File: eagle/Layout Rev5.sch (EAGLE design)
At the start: 12 parts, among them Q1 TIP122

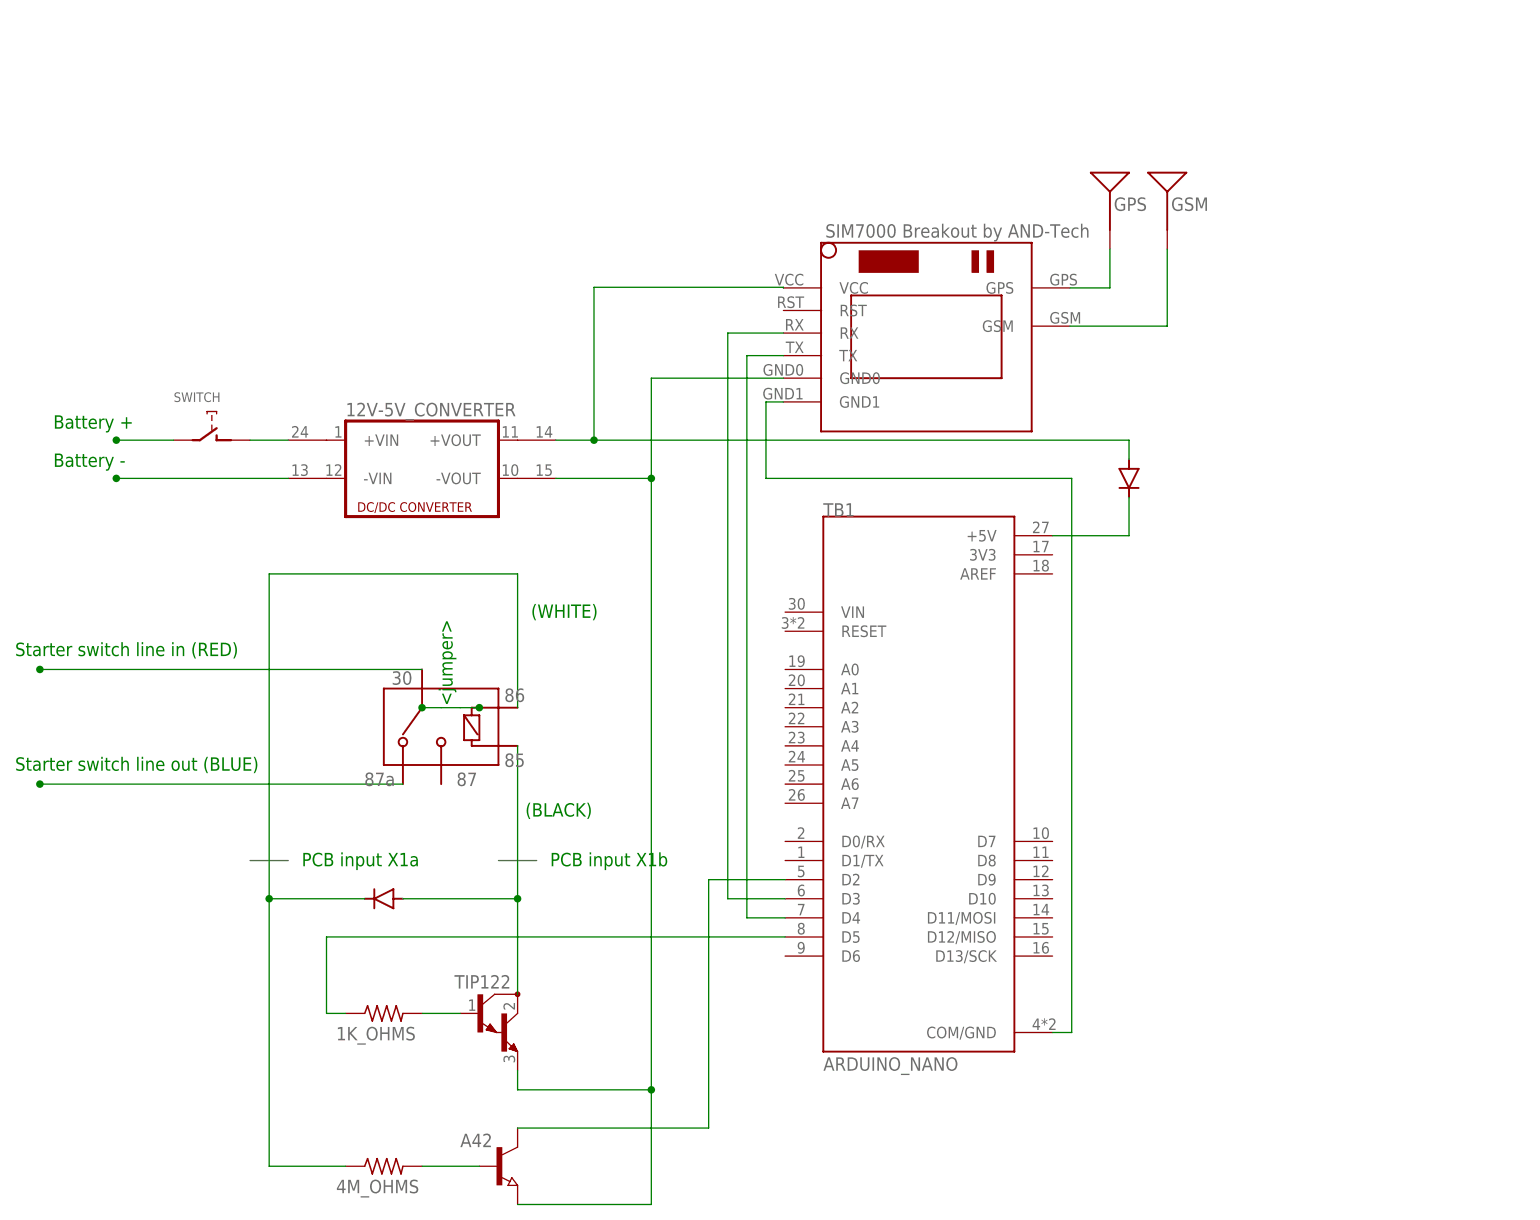
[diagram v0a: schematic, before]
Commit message: both bostig and stock: 1.change 10K resistor to 4M Ohm 2.make wiring look more like reality so building the hardware is more clear/intuitive including adding jumpers and inputs to PCB
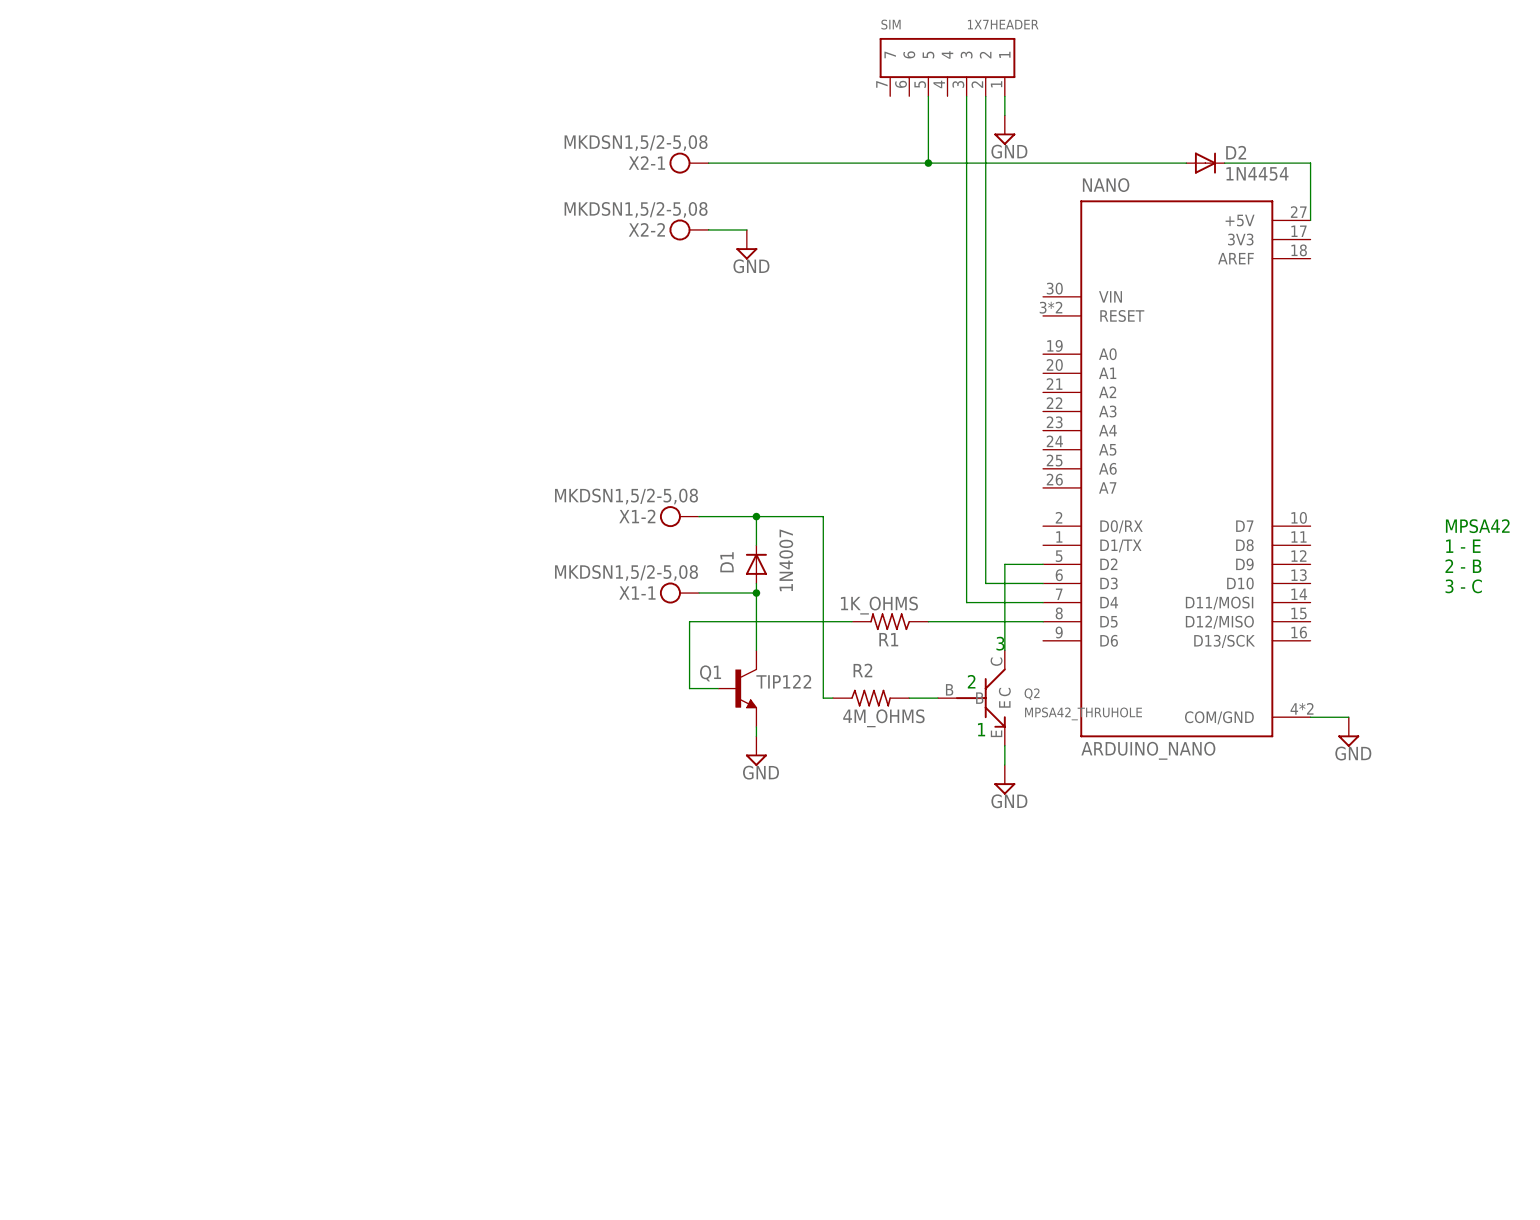
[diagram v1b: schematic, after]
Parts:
- removed 12V-5V_CONVERTER: (no value), dc-dc-converter:DC213R
- removed 1K_OHMS, 4M_OHMS: (no value), rcl:R-US_0411/15
- removed A42: (no value), semicon-smd-ipc:NPN-TRANSISTOR_SOT23
- removed GPS, GSM: 1.575GHz, SparkFun-GPS:ANTENNAGPS-2X7MM
- removed SWITCH: EC12E_SW, switch-alps:EC12E_SW
- removed TB1: ARDUINO_NANO, ARDUINO_NANO:ARDUINO_NANO
- removed U$1: SIM800LMODULE, JW_SIM800LMODULE:SIM800LMODULE
- added NANO: ARDUINO_NANO, ARDUINO_NANO:ARDUINO_NANO
- added Q2: MPSA42_THRUHOLE, MPSA42_thruhole:MPSA42_THRUHOLE
- added R1: 1K_OHMS, rcl:R-US_0207/10
- added R2: 4M_OHMS, rcl:R-US_0207/10
- added SIM: 1X7HEADER, 1x7header:1X7HEADER
- added X1, X2: MKDSN1,5/2-5,08, con-phoenix-508:MKDSN1,5/2-5,08
- D1: value 1N5400 -> 1N4007; device diode:1N5400 -> diode:1N4004
- D2: value 1N5400 -> 1N4454; device diode:1N5400 -> diode:1N4004
- Q1: device transistor-npn:TIP122 -> transistor:2SC1306
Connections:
- removed net N$11: TB1.D3, U$1.RX
- removed net N$12: TB1.D4, U$1.TX
- removed net N$13: 12V-5V_CONVERTER.+VIN1, SWITCHG$2.1
- removed net N$14: 4M_OHMS.2, A42.B
- removed net N$17: 4M_OHMS.1, D1.C
- removed net N$22: TB1.COM/GND, U$1.GND1
- removed net N$23: 12V-5V_CONVERTER.-VOUT1, A42.E, Q1.E, U$1.GND0
- removed net N$6: 1K_OHMS.1, TB1.D5
- removed net N$9: 12V-5V_CONVERTER.+VOUT1, D2.A, U$1.VCC
- new net +5V: D2.A, SIM.5, X2-1.KL
- new net GND: NANO.COM/GND, Q1.E, Q2.E, SIM.1, X2-2.KL
- new net N$7: Q2.B, R2.2
- net N$1: now also NANO.D4, SIM.3; no longer SWITCHG$2.2
- net N$10: now also NANO.+5V; no longer TB1.+5V
- net N$15: now also NANO.D2, Q2.C; no longer A42.C, TB1.D2
- net N$16: now also R1.2; no longer 1K_OHMS.2
- net N$2: now also NANO.D3, SIM.2; no longer 12V-5V_CONVERTER.-VIN1
- net N$3: now also D1.C, R2.1, X1-2.KL; no longer GSM.SIGNAL, U$1.GSM
- net N$4: now also NANO.D5, R1.1; no longer GPS.SIGNAL, U$1.GPS
- net N$5: now also X1-1.KL
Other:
- note added: "1"
- note added: "2"
- note added: "3"
- note added: "MPSA42 1 - E 2 - B 3 - C"
- note removed: "(BLACK)"
- note removed: "(WHITE)"
- note removed: "<jumper>"
- note removed: "Battery +"
- note removed: "Battery -"
- note removed: "PCB input X1a"
- note removed: "PCB input X1b"
- note removed: "Starter switch line in (RED)"
- note removed: "Starter switch line out (BLUE)"
